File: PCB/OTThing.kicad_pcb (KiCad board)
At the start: 2 copper layers, 51.5 x 71 mm, 95 parts, among them IC1 TPS61041, J3 USB_C_Receptacle_USB2.0, K1 G6K-2F-Y-5V, Q1 BC857C, Q10 BC847C, Q11 BC857C, Q12 BC847C, Q2 BC847C, Q4 BC857C, Q5 BC857C, Q6 BC857C, Q7 BC857C, Q8 BC847C, Q9 BC847C, SW1 RST/CONFIG, SW2 BOOT, U1 ESP32-C3-WROOM-02, U5 USBLC6-2SC6, U6 AMS1117-3.3

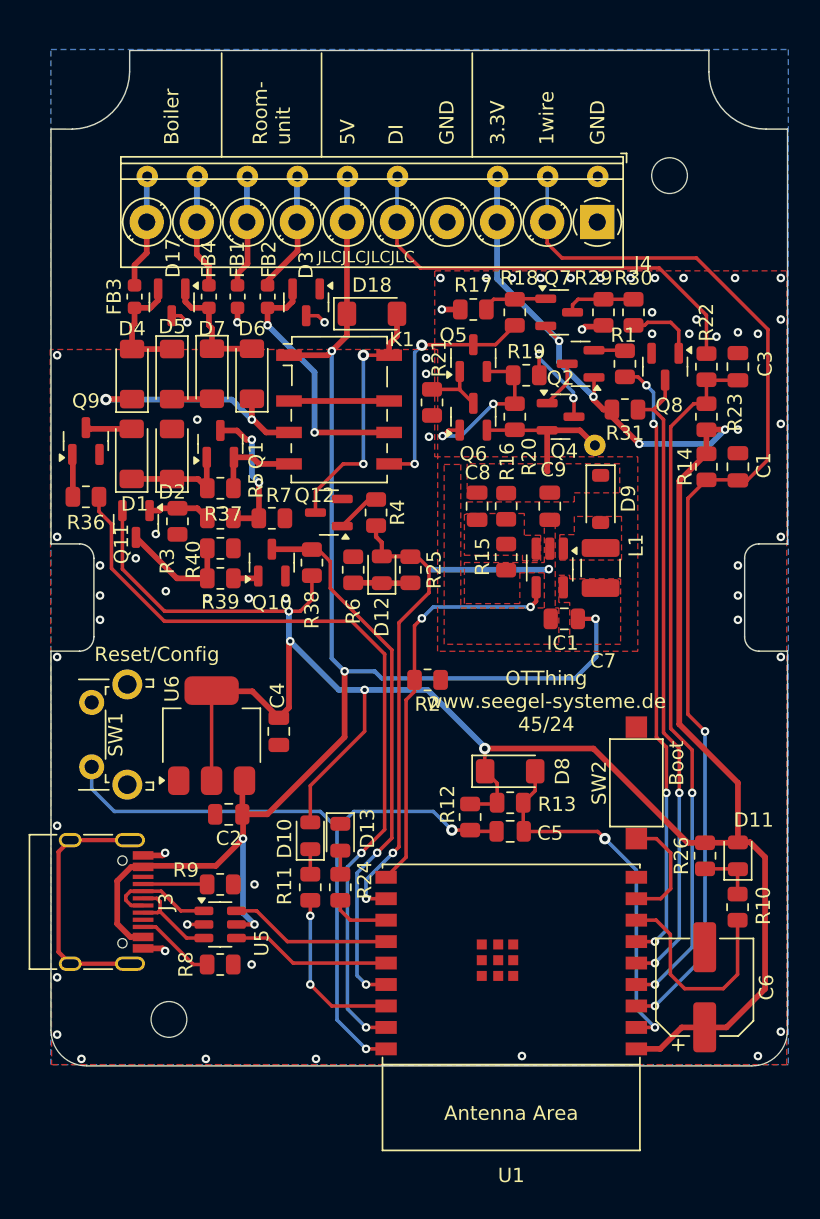
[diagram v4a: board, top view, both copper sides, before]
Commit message: add LED for +24V enable
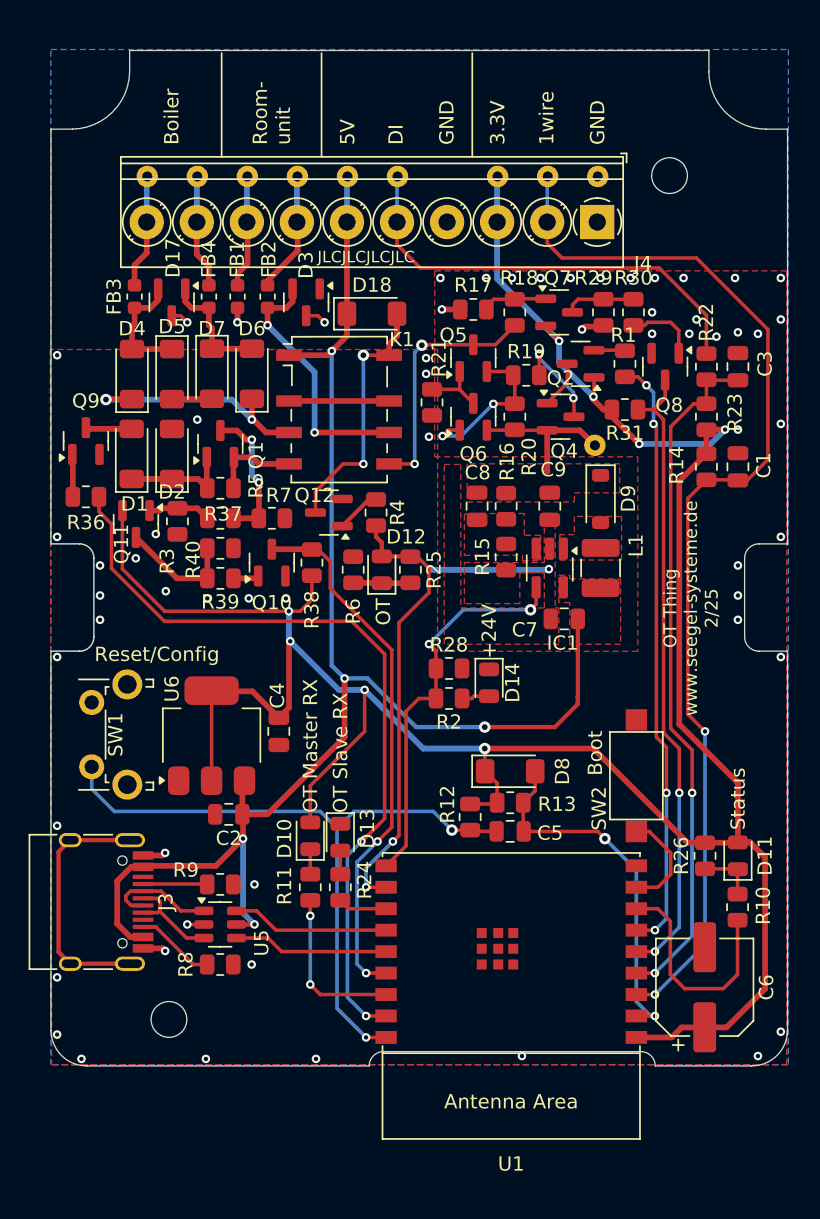
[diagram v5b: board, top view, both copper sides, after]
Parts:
- added D14: YL, LED_SMD:LED_0805_2012Metric, F.Cu at (145.9, 118.6)
- added R28: 12k, Resistor_SMD:R_0805_2012Metric, F.Cu at (143.1, 117.6)
- R10, R11, R24, R6: value 100 -> 120
- R2: value 33k -> 120
- moved R2 1.98 mm to (143.1, 119.7)
- moved U1 0.80 mm to (147.5, 137.5)
- moved SW2 0.50 mm to (156.2, 125.1)
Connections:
- R2 pad 1: GND -> Net-(D14-A)
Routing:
- net +5V: track 101.8 -> 103.8 mm
- net Net-(D14-A): track 0.00 -> 1.95 mm
- net /EN24: track 28.6 -> 27.7 mm
- net Net-(U1-GPIO8): track 14.8 -> 15.7 mm
- net Net-(U1-GPIO5/ADC2_CH0): track 49.1 -> 48.3 mm
- net /REL: track 32.3 -> 31.5 mm
- net /DQ: track 77.2 -> 76.4 mm
- net /OTS_TX: track 42.9 -> 42.1 mm
- net /OTS_RX: track 44.9 -> 44.1 mm
- net /OTM_RX: track 38.5 -> 37.7 mm
- net /CFG: track 49.7 -> 48.9 mm
- net /OTM_TX: track 56.1 -> 55.3 mm
- net Net-(U1-GPIO9): track 8.00 -> 7.29 mm
- net Net-(U1-GPIO21/U0TXD): track 4.15 -> 3.44 mm
- net /EN: track 26.4 -> 25.8 mm
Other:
- outline, holes or cut-outs redrawn
- board text added: "+24V"
- board text added: "OT"
- board text added: "OT Master RX"
- board text added: "OT Slave RX"
- board text added: "OT Thing www.seegel-systeme.de 2/25"
- board text added: "Status"
- board text removed: "OTThing www.seegel-systeme.de 45/24"

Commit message: migrate to pioarduino smart power add more OT values new partitiontable
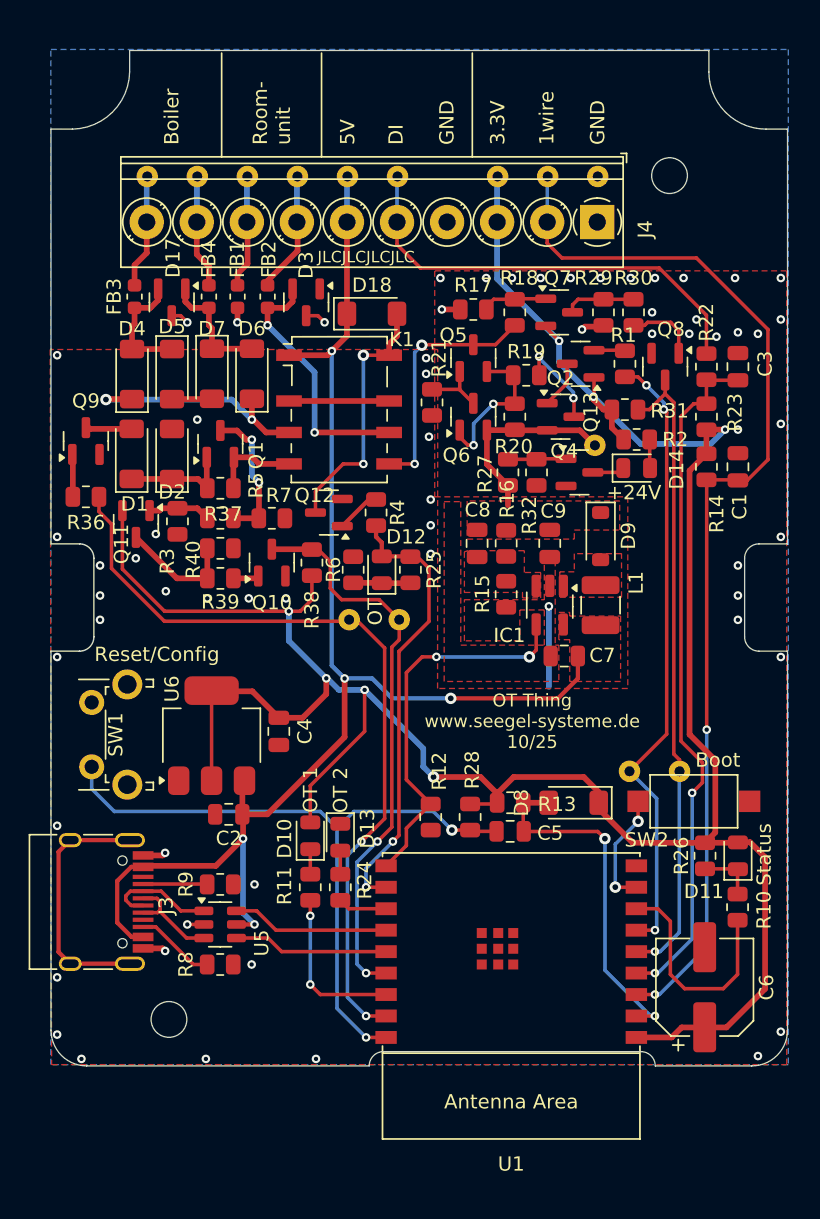
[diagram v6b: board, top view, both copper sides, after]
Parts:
- added Q13: BC847C, Package_TO_SOT_SMD:SOT-23, F.Cu at (152.2, 103.9)
- added R27: 33k, Resistor_SMD:R_0805_2012Metric, F.Cu at (147.2, 103.9)
- added R32: 1k, Resistor_SMD:R_0805_2012Metric, F.Cu at (149.2, 103.9)
- added TP11: ~, TestPoint:TestPoint_THTPad_D1.5mm_Drill0.7mm, B.Cu at (136.1, 114.2)
- added TP12: ~, TestPoint:TestPoint_THTPad_D1.5mm_Drill0.7mm, B.Cu at (139.6, 114.2)
- added TP13: ~, TestPoint:TestPoint_THTPad_D1.5mm_Drill0.7mm, B.Cu at (155.7, 124.8)
- added TP14: ~, TestPoint:TestPoint_THTPad_D1.5mm_Drill0.7mm, B.Cu at (159.2, 124.8)
- R20: value 100 -> 82
- moved R2 22.4 mm to (156.2, 101.6)
- moved D14 18.2 mm to (156.2, 103.6), turned to 0 degrees
- moved R28 10.5 mm to (141.8, 128.0), turned to -90 degrees
- moved D8 4.96 mm to (151.8, 127.0), turned to 180 degrees
- moved SW2 4.40 mm to (160.2, 126.9), turned to 0 degrees
- moved C7 2.60 mm to (151.2, 116.7)
- moved IC1 2.60 mm to (150.2, 113.2)
- moved L1 2.60 mm to (153.7, 113.2)
- moved R15 2.60 mm to (147.1, 112.4)
- moved C8 2.60 mm to (145.1, 108.9)
- moved C9 2.60 mm to (150.2, 108.9)
- moved D9 2.60 mm to (153.7, 108.4)
- moved R16 2.60 mm to (147.1, 108.9)
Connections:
- D14 pad 1: GND -> Net-(D14-K)
- R2 pad 2: /EN24 -> +3.3V
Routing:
- net +5V: track 103.8 -> 98.4 mm
- net Net-(Q13-B): track 0.00 -> 4.08 mm
- net +24V: track 10.9 -> 13.9 mm
- net GND: track 22.4 -> 19.5 mm, vias 62 -> 64
- net Net-(D14-K): track 0.00 -> 2.25 mm
- net /OTM_RX: track 37.7 -> 39.6 mm
- net /OTS_TX: track 42.1 -> 43.6 mm, vias 4 -> 3
- net +3.3V: track 181.7 -> 182.9 mm, vias 8 -> 7
- net /OTS_RX: track 44.1 -> 45.1 mm, vias 2 -> 1
- net Net-(U1-GPIO9): track 7.29 -> 8.14 mm, vias 0 -> 2
- net /DQ: track 76.4 -> 75.6 mm
- net /EN: track 25.8 -> 25.0 mm
- net Net-(Q5-E): track 11.3 -> 10.6 mm
- net /EN24: track 27.7 -> 27.0 mm
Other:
- board text added: "OT 1"
- board text added: "OT 2"
- board text added: "OT Thing www.seegel-systeme.de 10/25"
- board text removed: "OT Master RX"
- board text removed: "OT Slave RX"
- board text removed: "OT Thing www.seegel-systeme.de 2/25"

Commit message: Migrate to KiCad 9.0
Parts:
- R20: value 82 -> 100

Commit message: add USB test points single board test w/ power supply
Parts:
- added TP15: ~, TestPoint:TestPoint_THTPad_D1.5mm_Drill0.7mm, B.Cu at (124.9, 137.0)
- added TP16: ~, TestPoint:TestPoint_THTPad_D1.5mm_Drill0.7mm, B.Cu at (124.9, 134.0)
- moved R9 0.92 mm to (128.0, 132.7)
- moved U5 0.92 mm to (128.0, 135.5)
- moved R8 0.92 mm to (128.0, 138.3)
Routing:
- net Net-(J3-D+-PadA6): track 6.56 -> 8.66 mm
- net Net-(J3-CC2): track 5.57 -> 6.95 mm
- net Net-(J3-CC1): track 4.49 -> 5.40 mm
- net Net-(J3-D--PadA7): track 7.83 -> 8.75 mm
- net /DP: track 10.9 -> 9.94 mm
- net /DM: track 11.0 -> 10.1 mm
- net +5V: track 98.4 -> 99.2 mm
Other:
- board text added: "OT Thing www.seegel-systeme.de 15/25"
- board text removed: "OT Thing www.seegel-systeme.de 10/25"
